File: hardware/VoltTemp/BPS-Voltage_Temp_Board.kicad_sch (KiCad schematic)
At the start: 9 parts, among them J5 I-CAN connector, J6 I-CAN connector, U5 PeripheralSOM

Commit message: progress
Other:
- sheet TemperatureConn ports: added rawTemperature[0..4]; removed none
- sheet TemperatureFilters ports: added Temperatures[0..4], rawTemperature[0..4]; removed none
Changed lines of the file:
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@@
 	(wire
 		(pts
-			(xy 100.33 38.1) (xy 101.6 38.1)
-		)
-		(stroke
-			(width 0)
-			(type default)
-		)
-	)
-	(wire
-		(pts
 			(xy 274.32 29.21) (xy 274.32 31.75)
 		)
@@
 	(wire
 		(pts
-			(xy 101.6 38.1) (xy 102.87 39.37)
+			(xy 118.11 38.1) (xy 119.38 39.37)
 		)
 		(stroke
@@
 		)
 	)
+	(bus
+		(pts
+			(xy 48.26 58.42) (xy 69.85 58.42)
+		)
+		(stroke
+			(width 0)
+			(type default)
+		)
+	)
 	(wire
 		(pts
@@
 		)
 	)
+	(wire
+		(pts
+			(xy 115.316 38.1) (xy 118.11 38.1)
+		)
+		(stroke
+			(width 0)
+			(type default)
+		)
+	)
 	(bus
 		(pts
@@
 	(symbol
 		(lib_id "power:GND")
-		(at 102.87 39.37 0)
+		(at 119.38 39.37 0)
 		(unit 1)
 		(exclude_from_sim no)
@@
 		(fields_autoplaced yes)
 		(property "Reference" "#PWR026"
-			(at 102.87 45.72 0)
+			(at 119.38 45.72 0)
 			(effects
 				(font
@@
 		)
 		(property "Value" "GND"
-			(at 102.87 44.45 0)
+			(at 119.38 44.45 0)
 			(effects
 				(font
@@
 		)
 		(property "Footprint" ""
-			(at 102.87 39.37 0)
+			(at 119.38 39.37 0)
 			(effects
 				(font
@@
 		)
 		(property "Datasheet" ""
-			(at 102.87 39.37 0)
+			(at 119.38 39.37 0)
 			(effects
 				(font
@@
 		)
 		(property "Description" "Power symbol creates a global label with name \"GND\" , ground"
-			(at 102.87 39.37 0)
+			(at 119.38 39.37 0)
 			(effects
 				(font
@@
 	)
 	(sheet
-		(at 29.21 27.686)
-		(size 19.05 12.7)
+		(at 26.162 27.686)
+		(size 22.098 12.7)
 		(exclude_from_sim no)
 		(in_bom yes)
@@
 		)
 		(property "Sheetname" "VoltageConn"
-			(at 29.21 26.9744 0)
+			(at 26.162 26.9744 0)
 			(effects
 				(font
@@
 		)
 		(property "Sheetfile" "VoltageConn.kicad_sch"
-			(at 29.21 40.894 0)
+			(at 26.162 40.894 0)
 			(effects
 				(font
@@
 	(sheet
 		(at 69.85 27.686)
-		(size 30.48 16.764)
+		(size 45.466 16.764)
 		(exclude_from_sim no)
 		(in_bom yes)
@@
 		)
 		(pin "bmsEn" input
-			(at 100.33 33.02 0)
+			(at 115.316 33.02 0)
 			(effects
 				(font
@@
 		)
 		(pin "LV_RTN" bidirectional
-			(at 100.33 38.1 0)
+			(at 115.316 38.1 0)
 			(effects
 				(font
@@
 		)
 		(pin "{I2C}" bidirectional
-			(at 100.33 30.48 0)
+			(at 115.316 30.48 0)
 			(effects
 				(font
@@
 		)
 		(pin "bmsAlert" output
-			(at 100.33 35.56 0)
+			(at 115.316 35.56 0)
 			(effects
 				(font
@@
 	)
 	(sheet
-		(at 29.21 55.118)
-		(size 22.86 7.62)
+		(at 26.416 55.118)
+		(size 21.844 7.62)
 		(exclude_from_sim no)
 		(in_bom yes)
@@
 		)
 		(property "Sheetname" "TemperatureConn"
-			(at 29.21 54.4064 0)
+			(at 26.416 54.4064 0)
 			(effects
 				(font
@@
 		)
 		(property "Sheetfile" "TemperatureConn.kicad_sch"
-			(at 28.956 62.992 0)
+			(at 26.162 62.992 0)
 			(effects
 				(font
@@
 			)
 		)
+		(pin "rawTemperature[0..4]" bidirectional
+			(at 48.26 58.42 0)
+			(effects
+				(font
+					(size 1.27 1.27)
+				)
+				(justify right)
+			)
+		)
 		(instances
 			(project "BPS-Voltage_Temp_Board"
@@
 	)
 	(sheet
-		(at 52.832 80.264)
-		(size 26.67 7.62)
+		(at 69.85 54.864)
+		(size 45.466 7.62)
 		(exclude_from_sim no)
 		(in_bom yes)
@@
 		)
 		(property "Sheetname" "TemperatureFilters"
-			(at 52.832 79.5524 0)
+			(at 69.85 54.1524 0)
 			(effects
 				(font
@@
 		)
 		(property "Sheetfile" "TemperatureFilters.kicad_sch"
-			(at 52.832 88.138 0)
+			(at 69.85 62.738 0)
 			(effects
 				(font
@@
 			)
 		)
+		(pin "Temperatures[0..4]" output
+			(at 115.316 58.42 0)
+			(effects
+				(font
+					(size 1.27 1.27)
+				)
+				(justify right)
+			)
+		)
+		(pin "rawTemperature[0..4]" input
+			(at 69.85 58.42 180)
+			(effects
+				(font
+					(size 1.27 1.27)
+				)
+				(justify left)
+			)
+		)

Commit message: more progress on schematic
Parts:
- removed J5, J6: I-CAN connector, Connector_Molex:Molex_Nano-Fit_105313-xx04_1x04_P2.50mm_Horizontal, symbol utsvt-connectors:PeripheralCANConnector
- added J2, J3: PeripheralCAN, UTSVT_Connectors:Molex_Nano-Fit_105309-xx04_1x04_P2.50mm_Vertical, symbol utsvt_connectors:PeripheralCANConnector
- added J5: SFH11-PBPC-D05-ST-BK, CONN_SFH11-xxxC-D05-ST-XX_SUL, symbol utsvt_connectors:SFH11-PBPC-D05-ST-BK
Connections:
- net GNDPWR is gone; now on net GND: U5.24 (GNDPWR)
- net GND: now also J2.2 (GND), J3.2 (GND), J5.10 (GND), J5.9 (GND)
- net I-CAN_H: now also J2.3 (CAN_H), J3.3 (CAN_H)
- net I-CAN_L: now also J2.4 (CAN_L), J3.4 (CAN_L)
- net +12V renamed +24V
- net +24V: now also J2.1 (24V), J3.1 (24V)
- net psSCL renamed I2C_SCL
- net I2C_SCL: now also J5.2 (CH1)
- net psSDA renamed I2C_SDA
- net I2C_SDA: now also J5.1 (CH0)
- new net bmsAlert: J5.4 (CH3)
- new net bmsEn: J5.3 (CH2)
- no-connect marks 10 -> 14
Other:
- removed sheet Thermistor town
- sheet TemperatureFilters ports: added Temperature[0..4]; removed Temperatures[0..4]
- note added: "BPS-CAN Connectors"
- note added: "PSOM Connections"
- note removed: "I-CAN connectors"
- note removed: "Psom & ICAN Connectors"
- note removed: "Thermistor Town"
- moved on the sheet: MH1, MH2, MH3, MH4, U5

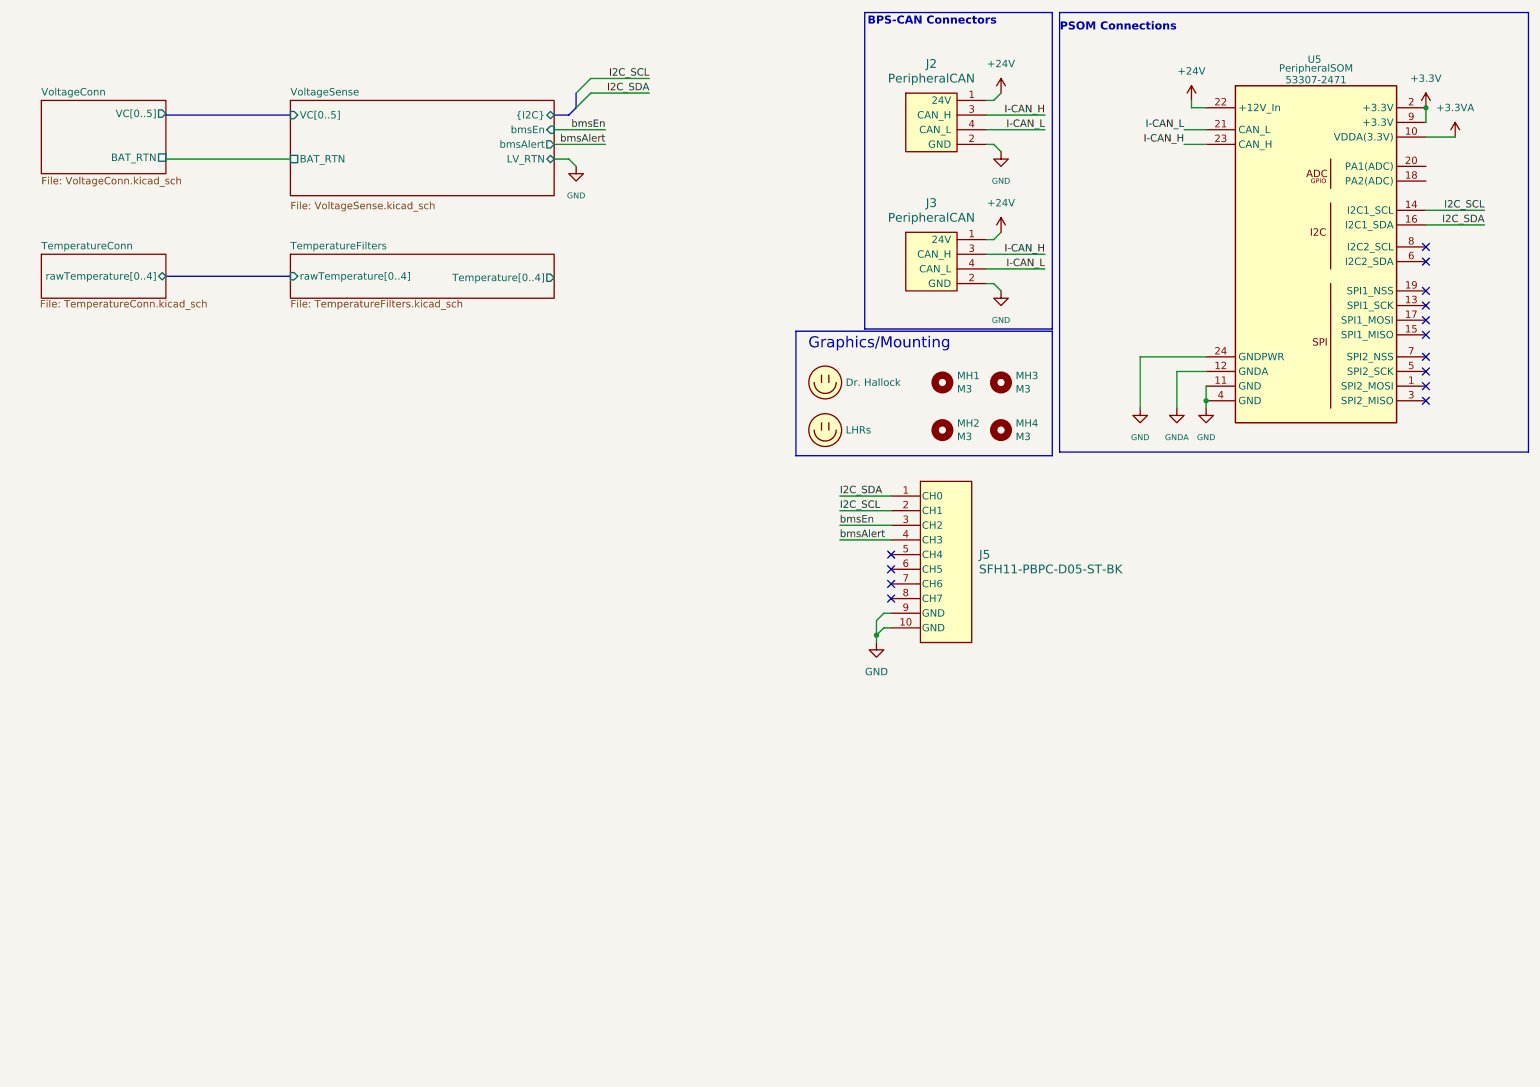
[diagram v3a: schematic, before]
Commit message: clean up schematic a lil bit
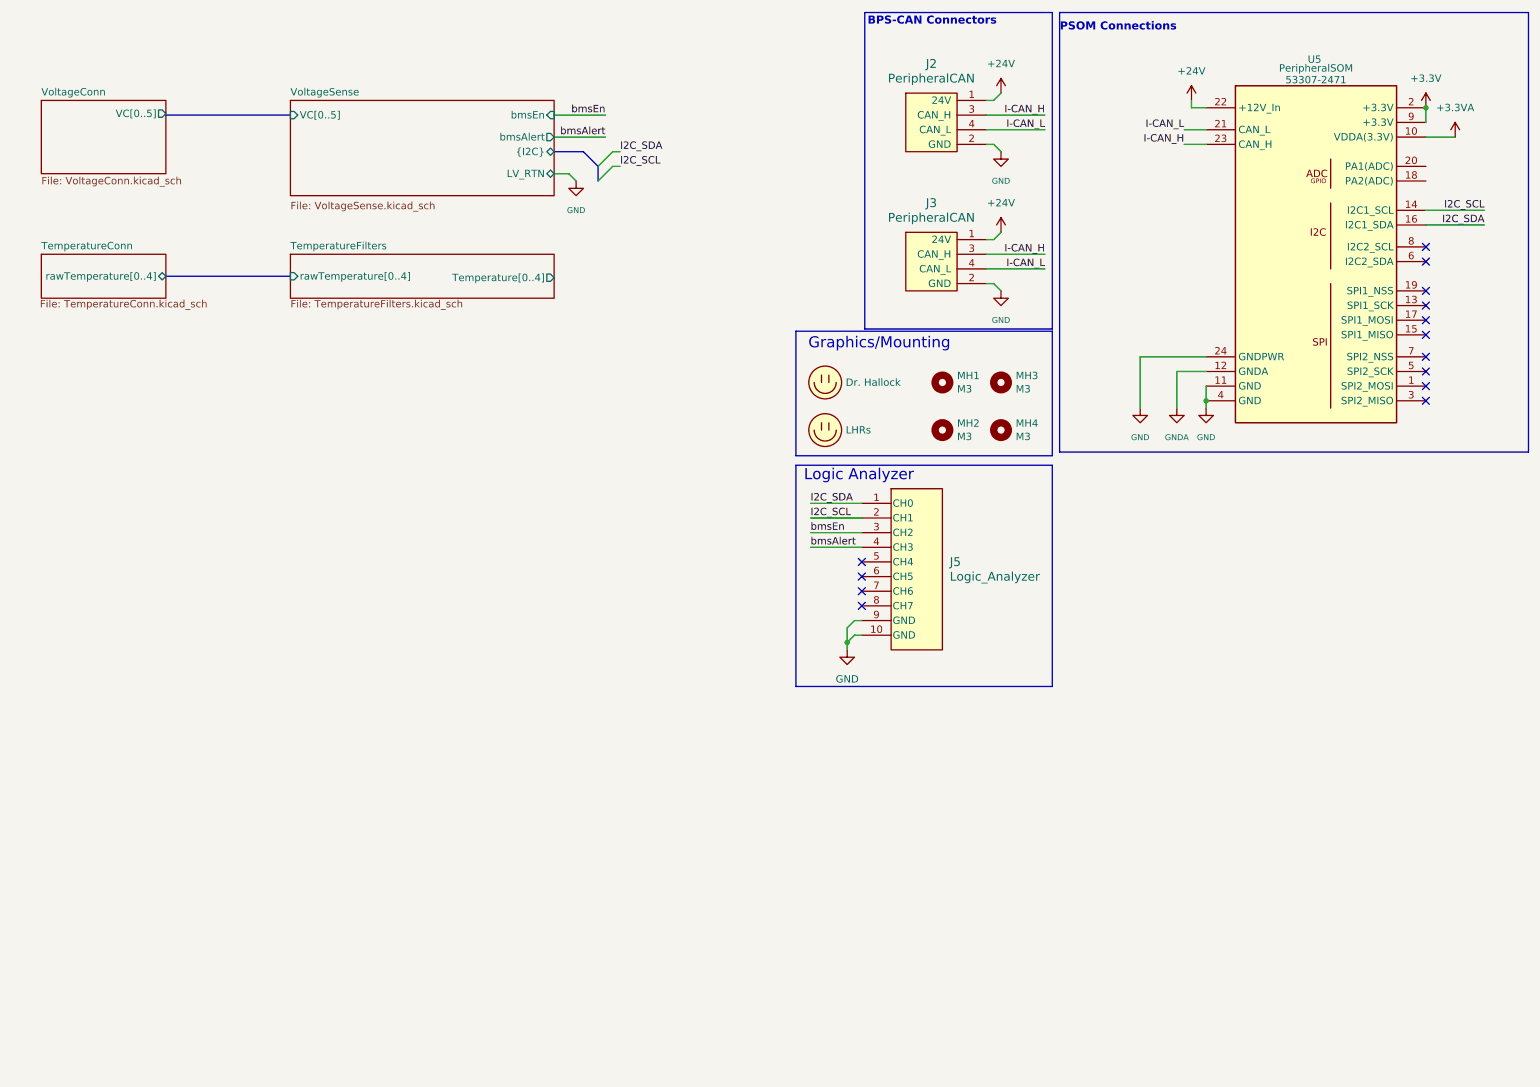
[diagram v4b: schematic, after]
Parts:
- J5: value SFH11-PBPC-D05-ST-BK -> Logic_Analyzer
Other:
- sheet VoltageConn ports: added none; removed BAT_RTN
- sheet VoltageSense ports: added none; removed BAT_RTN
- note added: "Logic Analyzer"
- moved on the sheet: J5
